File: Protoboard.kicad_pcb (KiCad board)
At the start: 2 copper layers, 36 x 48 mm, 11 parts, among them P1 CONN_01X08, P2 CONN_01X04, P3 CONN_01X05, P4 CONN_01X04, P5 CONN_02X05, P6 CONN_01X10

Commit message: Routing done.
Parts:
- removed P6: CONN_01X10, Pin_Headers:Pin_Header_Straight_1x10
- P4: value CONN_01X04 -> CONN_01X11; footprint Pin_Headers:Pin_Header_Straight_1x04 -> Pin_Headers:Pin_Header_Straight_1x11
- moved R1 109.8 mm to (232.0, 103.0), turned to 90 degrees
- moved D1 107.9 mm to (232.0, 118.0)
- moved P3 107.3 mm to (211.5, 128.0)
- moved D2 105.7 mm to (232.0, 122.0), turned to 90 degrees
- moved P2 103.0 mm to (225.0, 99.5), turned to 0 degrees
- moved P4 102.7 mm to (229.0, 93.9)
- moved R3 98.6 mm to (224.0, 118.0)
- moved R2 85.5 mm to (232.0, 112.0)
- moved P1 74.9 mm to (214.1, 103.5), turned to 180 degrees
- moved P5 70.3 mm to (173.7, 98.0)
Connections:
- D2 pad 1: (no net) -> LED
- P4 pad 1: GND -> SCL
- P4 pad 2: +3.3V -> SDA
- P4 pad 3: SCL -> +3.3V
- P4 pad 4: SDA -> GND
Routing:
- net +5V: track 0.00 -> 99.3 mm, vias 0 -> 2
- net RXD: track 0.00 -> 88.6 mm, vias 0 -> 2
- net TXD: track 0.00 -> 86.2 mm, vias 0 -> 2
- net GND: track 0.00 -> 83.8 mm, vias 0 -> 2
- net RESET: track 0.00 -> 70.6 mm
- net SET: track 0.00 -> 62.2 mm, vias 0 -> 2
- net +3.3V: track 0.00 -> 29.1 mm
- net (no net): track 0.00 -> 19.5 mm
- net DIN: track 0.00 -> 10.8 mm
- net SCL: track 0.00 -> 5.48 mm
- net LED: track 0.00 -> 5.28 mm
- net SDA: track 0.00 -> 4.92 mm
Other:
- board size 36 x 48 mm -> 65 x 50 mm
- net class Default: via_dia 0.6 -> 1.2; via_drill 0.4 -> 0.5

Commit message: Generated drill files and stencils.
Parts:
- added D1: D, Diodes_SMD:SOD-323_HandSoldering, F.Cu at (152.0, 103.0)
- added D1: D, Diodes_SMD:SOD-323_HandSoldering, F.Cu at (82.0, 103.0)
- added D1: D, Diodes_SMD:SOD-323_HandSoldering, F.Cu at (152.0, 48.0)
- added D2: D, Diodes_SMD:SOD-323_HandSoldering, F.Cu at (152.0, 107.0)
- added D2: D, Diodes_SMD:SOD-323_HandSoldering, F.Cu at (82.0, 107.0)
- added D2: D, Diodes_SMD:SOD-323_HandSoldering, F.Cu at (152.0, 52.0)
- added P1: CONN_01X08, Connectors_Molex:Molex_PicoBlade_53261-0871_08x1.25mm_Angled, F.Cu at (134.1, 88.5)
- added P1: CONN_01X08, Connectors_Molex:Molex_PicoBlade_53261-0871_08x1.25mm_Angled, F.Cu at (64.1, 88.5)
- added P1: CONN_01X08, Connectors_Molex:Molex_PicoBlade_53261-0871_08x1.25mm_Angled, F.Cu at (134.1, 33.5)
- added P2: CONN_01X04, Pin_Headers:Pin_Header_Straight_1x04, B.Cu at (145.0, 84.5)
- added P2: CONN_01X04, Pin_Headers:Pin_Header_Straight_1x04, B.Cu at (75.0, 84.5)
- added P2: CONN_01X04, Pin_Headers:Pin_Header_Straight_1x04, B.Cu at (145.0, 29.5)
- added P3: CONN_01X05, Connectors_JST:JST_XH_S05B-XH-A_05x2.50mm_Angled, F.Cu at (131.5, 113.0)
- added P3: CONN_01X05, Connectors_JST:JST_XH_S05B-XH-A_05x2.50mm_Angled, F.Cu at (61.5, 113.0)
- added P3: CONN_01X05, Connectors_JST:JST_XH_S05B-XH-A_05x2.50mm_Angled, F.Cu at (131.5, 58.0)
- added P4: CONN_01X11, Pin_Headers:Pin_Header_Straight_1x11, B.Cu at (149.0, 78.9)
- added P4: CONN_01X11, Pin_Headers:Pin_Header_Straight_1x11, B.Cu at (79.0, 78.9)
- added P4: CONN_01X11, Pin_Headers:Pin_Header_Straight_1x11, B.Cu at (149.0, 23.9)
- added P5: CONN_02X05, Amphenol:Amphenol, F.Cu at (93.7, 83.0)
- added P5: CONN_02X05, Amphenol:Amphenol, F.Cu at (23.7, 83.0)
- added P5: CONN_02X05, Amphenol:Amphenol, F.Cu at (93.7, 28.1)
- added R1: 10k, Resistors_SMD:R_1206_HandSoldering, F.Cu at (152.0, 88.0)
- added R1: 10k, Resistors_SMD:R_1206_HandSoldering, F.Cu at (82.0, 88.0)
- added R1: 10k, Resistors_SMD:R_1206_HandSoldering, F.Cu at (152.0, 33.0)
- added R2: 10k, Resistors_SMD:R_1206_HandSoldering, F.Cu at (152.0, 97.0)
- added R2: 10k, Resistors_SMD:R_1206_HandSoldering, F.Cu at (82.0, 97.0)
- added R2: 10k, Resistors_SMD:R_1206_HandSoldering, F.Cu at (152.0, 42.0)
- added R3: 10k, Resistors_SMD:R_1206_HandSoldering, F.Cu at (144.0, 103.0)
- added R3: 10k, Resistors_SMD:R_1206_HandSoldering, F.Cu at (74.0, 103.0)
- added R3: 10k, Resistors_SMD:R_1206_HandSoldering, F.Cu at (144.0, 48.0)
- moved D1 165.5 mm to (82.0, 48.0)
- moved D2 165.5 mm to (82.0, 52.0)
- moved P1 165.5 mm to (64.1, 33.5)
- moved P2 165.5 mm to (75.0, 29.5)
- moved P3 165.5 mm to (61.5, 58.0)
- moved P4 165.5 mm to (79.0, 23.9)
- moved P5 165.5 mm to (23.7, 28.1)
- moved R1 165.5 mm to (82.0, 33.0)
- moved R2 165.5 mm to (82.0, 42.0)
- moved R3 165.5 mm to (74.0, 48.0)
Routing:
- net +5V: track 99.3 -> 397.3 mm, vias 2 -> 8
- net RXD: track 88.6 -> 354.3 mm, vias 2 -> 8
- net TXD: track 86.2 -> 344.6 mm, vias 2 -> 8
- net GND: track 83.8 -> 335.2 mm, vias 2 -> 8
- net RESET: track 70.6 -> 282.6 mm
- net SET: track 62.2 -> 248.9 mm, vias 2 -> 8
- net +3.3V: track 29.1 -> 116.3 mm
- net (no net): track 19.5 -> 78.0 mm
- net DIN: track 10.8 -> 43.4 mm
- net SCL: track 5.48 -> 21.9 mm
- net LED: track 5.28 -> 21.1 mm
- net SDA: track 4.92 -> 19.7 mm
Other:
- board size 65 x 50 mm -> 135 x 105 mm

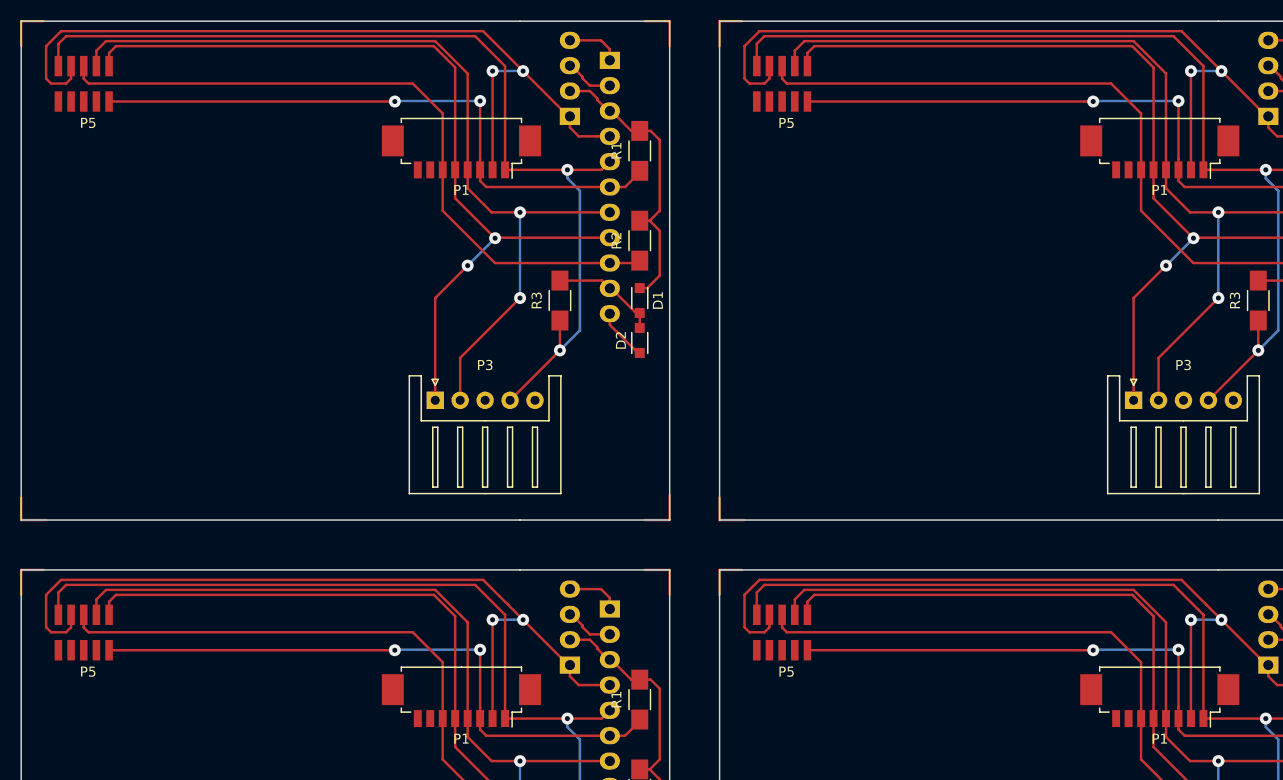
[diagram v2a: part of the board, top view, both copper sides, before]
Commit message: Moved tracks around.
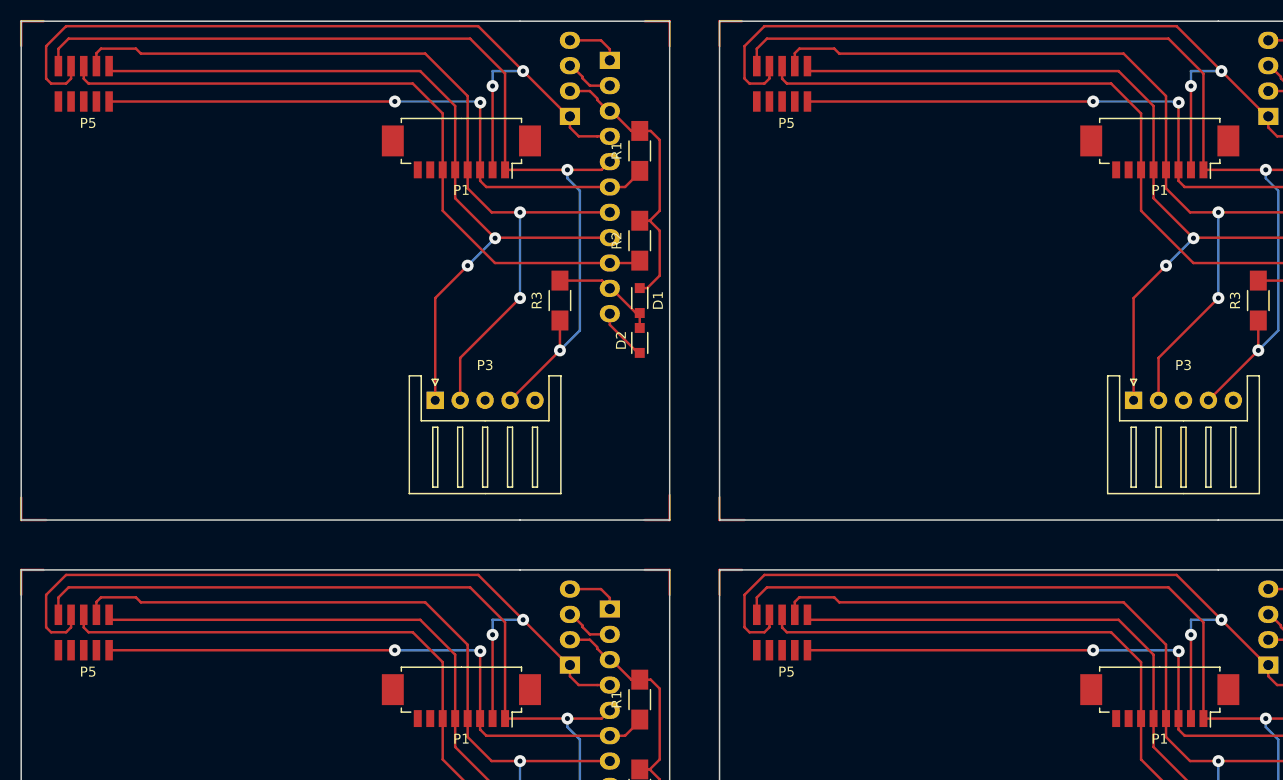
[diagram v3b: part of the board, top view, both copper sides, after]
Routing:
- net TXD: track 344.6 -> 326.6 mm
- net RXD: track 354.3 -> 345.9 mm
- net +5V: track 397.3 -> 393.5 mm
- net GND: track 335.2 -> 336.9 mm

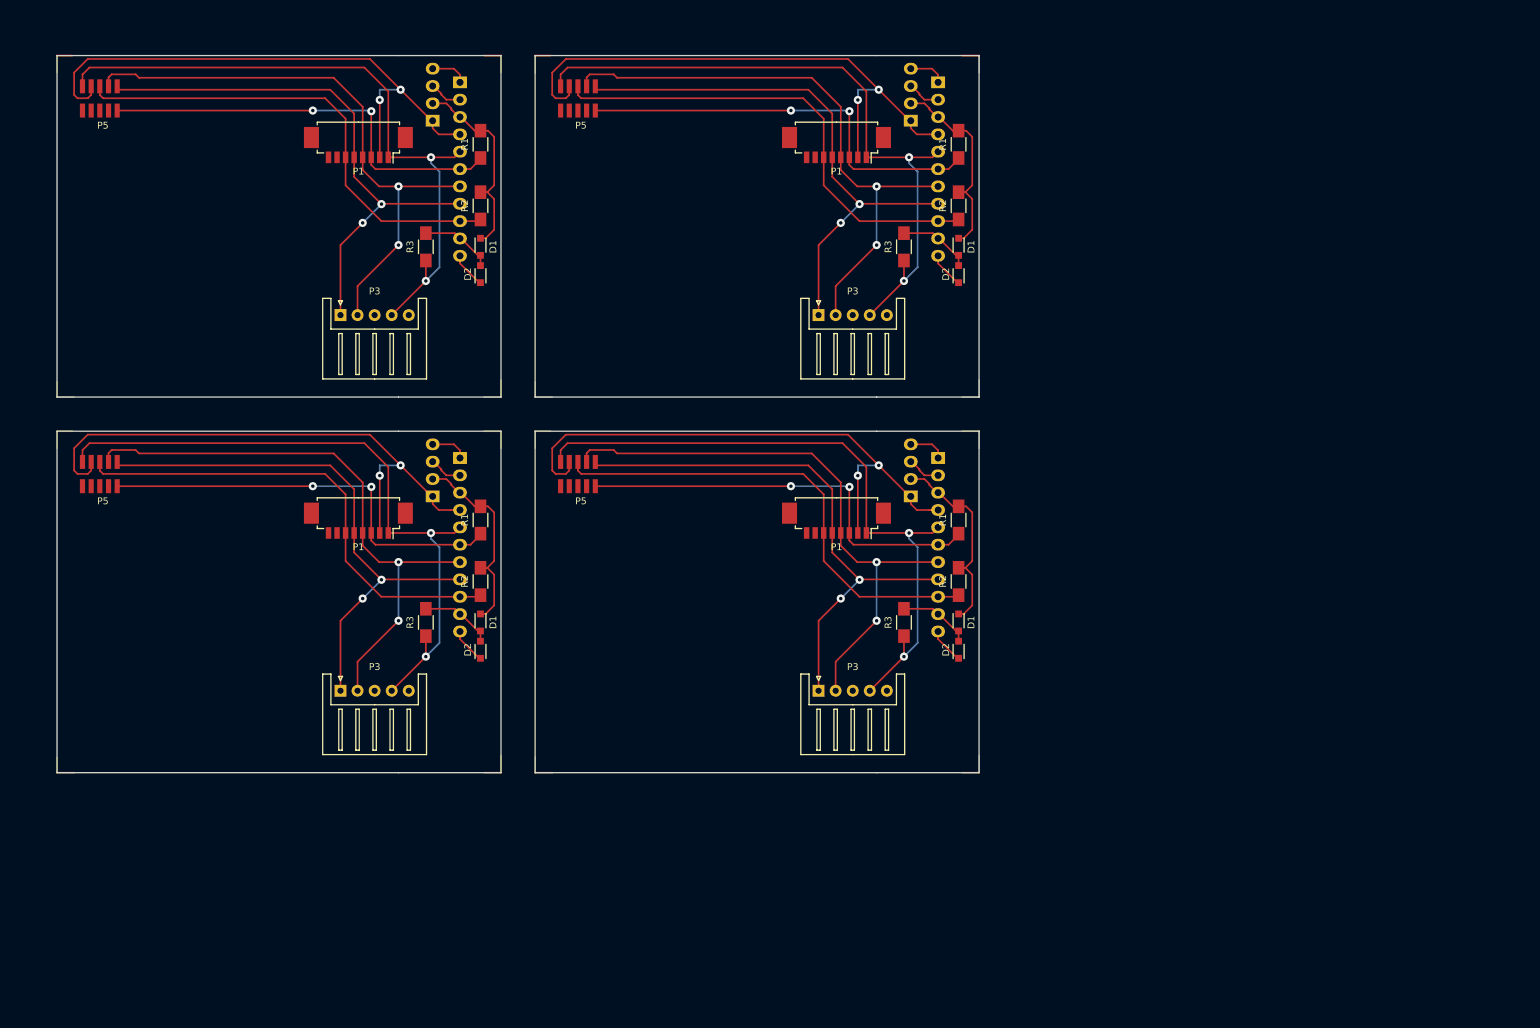
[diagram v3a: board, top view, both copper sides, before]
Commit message: Added holes to denote corners of the board. Regenerated outputs.
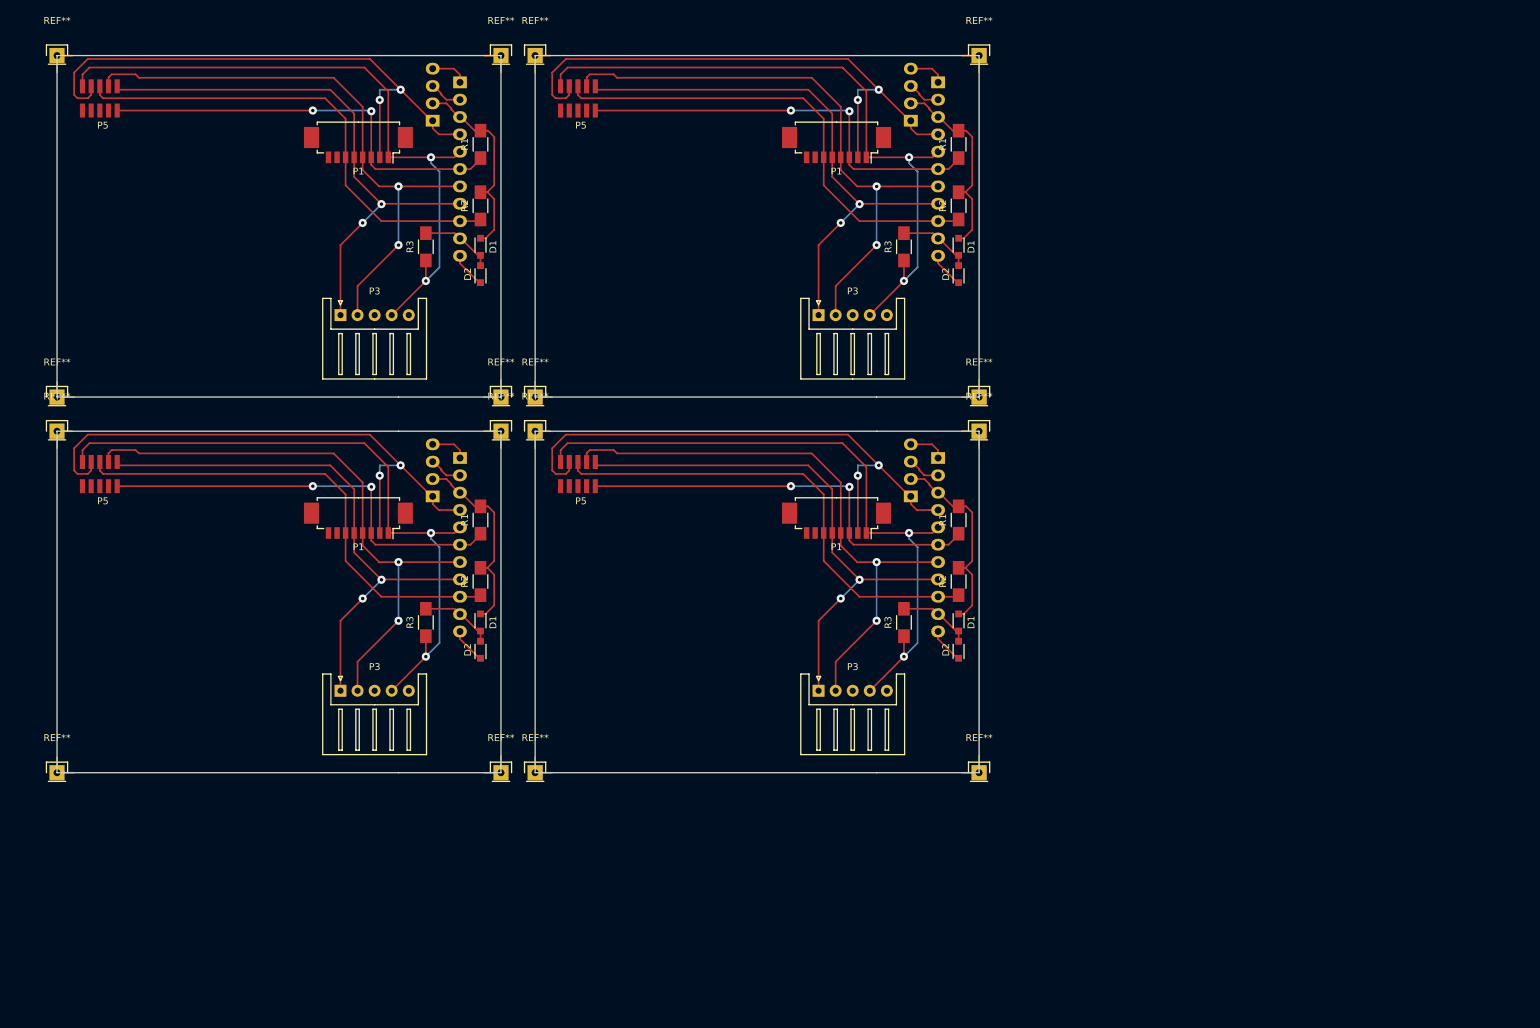
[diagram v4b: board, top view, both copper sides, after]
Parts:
- added REF**: Pin_Header_Straight_1x01, Pin_Headers:Pin_Header_Straight_1x01, F.Cu at (90.0, 75.0)
- added REF**: Pin_Header_Straight_1x01, Pin_Headers:Pin_Header_Straight_1x01, F.Cu at (155.0, 125.0)
- added REF**: Pin_Header_Straight_1x01, Pin_Headers:Pin_Header_Straight_1x01, F.Cu at (155.0, 70.0)
- added REF**: Pin_Header_Straight_1x01, Pin_Headers:Pin_Header_Straight_1x01, F.Cu at (85.0, 125.0)
- added REF**: Pin_Header_Straight_1x01, Pin_Headers:Pin_Header_Straight_1x01, F.Cu at (20.0, 20.0)
- added REF**: Pin_Header_Straight_1x01, Pin_Headers:Pin_Header_Straight_1x01, F.Cu at (20.0, 70.0)
- added REF**: Pin_Header_Straight_1x01, Pin_Headers:Pin_Header_Straight_1x01, F.Cu at (85.0, 20.0)
- added REF**: Pin_Header_Straight_1x01, Pin_Headers:Pin_Header_Straight_1x01, F.Cu at (85.0, 70.0)
- added REF**: Pin_Header_Straight_1x01, Pin_Headers:Pin_Header_Straight_1x01, F.Cu at (90.0, 20.0)
- added REF**: Pin_Header_Straight_1x01, Pin_Headers:Pin_Header_Straight_1x01, F.Cu at (20.0, 75.0)
- added REF**: Pin_Header_Straight_1x01, Pin_Headers:Pin_Header_Straight_1x01, F.Cu at (90.0, 125.0)
- added REF**: Pin_Header_Straight_1x01, Pin_Headers:Pin_Header_Straight_1x01, F.Cu at (90.0, 70.0)
- added REF**: Pin_Header_Straight_1x01, Pin_Headers:Pin_Header_Straight_1x01, F.Cu at (20.0, 125.0)
- added REF**: Pin_Header_Straight_1x01, Pin_Headers:Pin_Header_Straight_1x01, F.Cu at (155.0, 75.0)
- added REF**: Pin_Header_Straight_1x01, Pin_Headers:Pin_Header_Straight_1x01, F.Cu at (155.0, 20.0)
- added REF**: Pin_Header_Straight_1x01, Pin_Headers:Pin_Header_Straight_1x01, F.Cu at (85.0, 75.0)
